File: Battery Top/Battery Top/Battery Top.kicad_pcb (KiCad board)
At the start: 2 copper layers, 64 x 21 mm, 7 parts, among them J1 JST_PWR_CON, J2 VBAT+_2, J3 VBAT+_1, J4 GND_R, J5 DATA_1, J6 GND_L

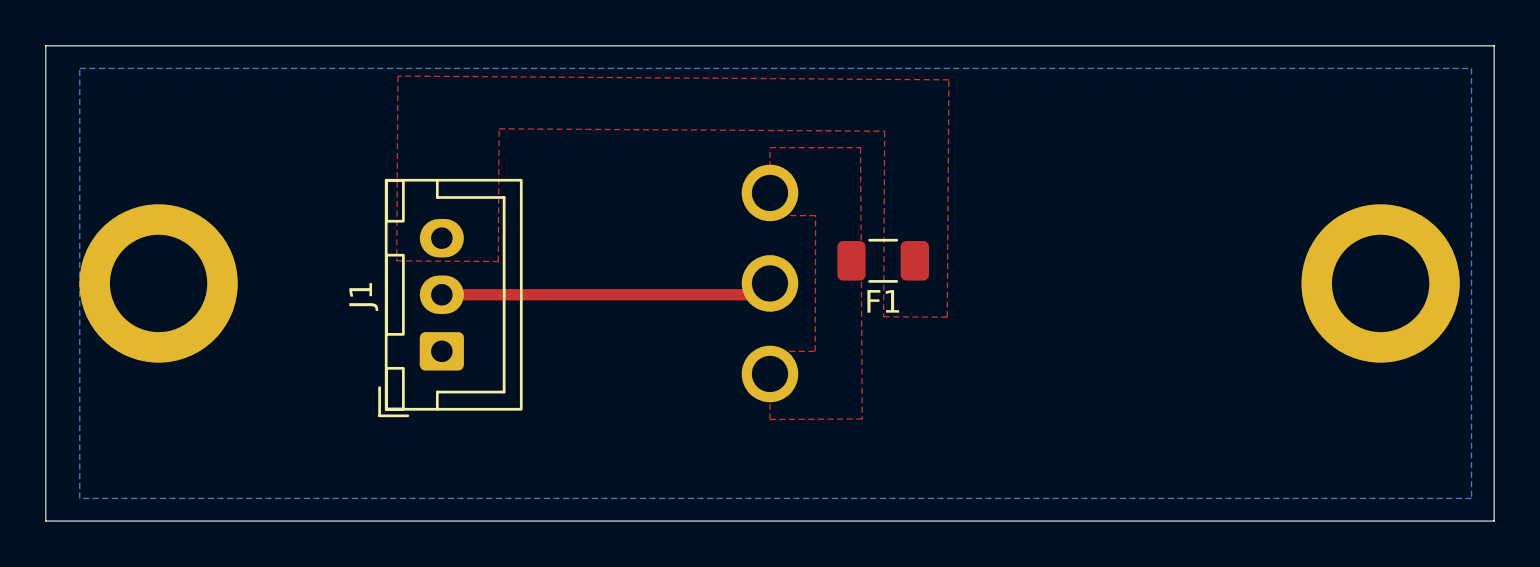
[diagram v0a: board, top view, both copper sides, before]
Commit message: fixed footprint for fuse
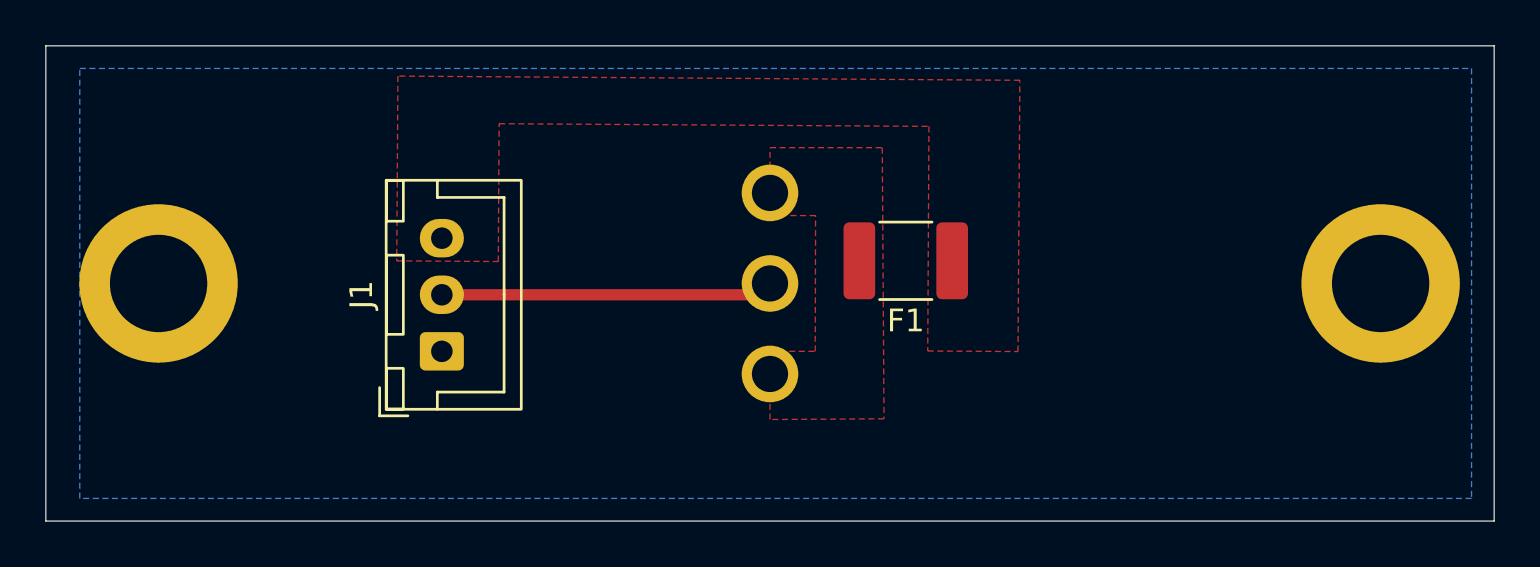
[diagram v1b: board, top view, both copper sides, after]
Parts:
- F1: footprint Fuse:Fuse_1206_3216Metric -> Capacitor_SMD:C_1812_4532Metric
- moved F1 1.00 mm to (157.0, 99.0)
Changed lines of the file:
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@@
 		)
 	)
-	(footprint "Fuse:Fuse_1206_3216Metric"
-		(layer "F.Cu")
-		(at 156 99 180)
-		(descr "Fuse SMD 1206 (3216 Metric), square (rectangular) end terminal, IPC-7351 nominal, (Body size source: http://www.tortai-tech.com/upload/download/2011102023233369053.pdf)")
-		(tags "fuse")
+	(footprint "Capacitor_SMD:C_1812_4532Metric"
+		(layer "F.Cu")
+		(at 157 99 180)
+		(descr "Capacitor SMD 1812 (4532 Metric), square (rectangular) end terminal, IPC-7351 nominal, (Body size source: IPC-SM-782 page 76, https://www.pcb-3d.com/wordpress/wp-content/uploads/ipc-sm-782a_amendment_1_and_2.pdf)")
+		(tags "capacitor")
 		(property "Reference" "F1"
-			(at 0 -1.83 180)
+			(at 0 -2.65 180)
 			(layer "F.SilkS")
 			(effects
@@
 		)
 		(property "Value" "FUSE_VBAT+_1"
-			(at 0 1.83 180)
+			(at 0 2.65 180)
 			(layer "F.Fab")
 			(effects
@@
 		(duplicate_pad_numbers_are_jumpers no)
 		(fp_line
-			(start -0.602064 0.91)
-			(end 0.602064 0.91)
+			(start -1.161252 1.71)
+			(end 1.161252 1.71)
 			(stroke
 				(width 0.12)
@@
 		)
 		(fp_line
-			(start -0.602064 -0.91)
-			(end 0.602064 -0.91)
+			(start -1.161252 -1.71)
+			(end 1.161252 -1.71)
 			(stroke
 				(width 0.12)
@@
 		)
 		(fp_rect
-			(start -2.28 -1.13)
-			(end 2.28 1.13)
+			(start -3 -1.95)
+			(end 3 1.95)
 			(stroke
 				(width 0.05)
@@
 		)
 		(fp_rect
-			(start -1.6 -0.8)
-			(end 1.6 0.8)
+			(start -2.25 -1.6)
+			(end 2.25 1.6)
 			(stroke
 				(width 0.1)
@@
 			(effects
 				(font
-					(size 0.8 0.8)
-					(thickness 0.12)
+					(size 1 1)
+					(thickness 0.15)
 				)
 			)
 		)
 		(pad "1" smd roundrect
-			(at -1.4 0 180)
-			(size 1.25 1.75)
+			(at -2.05 0 180)
+			(size 1.4 3.4)
 			(layers "F.Cu" "F.Mask" "F.Paste")
-			(roundrect_rratio 0.2)
+			(roundrect_rratio 0.178571)
 			(net "/VBAT+")
 			(pintype "passive")
 		)
 		(pad "2" smd roundrect
-			(at 1.4 0 180)
-			(size 1.25 1.75)
+			(at 2.05 0 180)
+			(size 1.4 3.4)
 			(layers "F.Cu" "F.Mask" "F.Paste")
-			(roundrect_rratio 0.2)
+			(roundrect_rratio 0.178571)
 			(net "/VBAT+_P")
 			(pintype "passive")
 		)
 		(embedded_fonts no)
-		(model "${KICAD10_3DMODEL_DIR}/Fuse.3dshapes/Fuse_1206_3216Metric.step"
+		(model "${KICAD10_3DMODEL_DIR}/Capacitor_SMD.3dshapes/C_1812_4532Metric.step"
 			(offset
 				(xyz 0 0 0)
@@
 		(polygon
 			(pts
-				(xy 153.01436 97.00265) (xy 151 96.997387) (xy 151 94) (xy 155 94) (xy 155.076836 105.986685) (xy 151 106.012822)
-				(xy 151 103.000002) (xy 152.998694 103)
+				(xy 153.01436 97.00265) (xy 151 96.997387) (xy 151 94) (xy 155.96154 94) (xy 156.038336 105.980521)
+				(xy 151 106.012822) (xy 151 103.000002) (xy 152.998694 103)
 			)
 		)
@@
 		(polygon
 			(pts
-				(xy 156.065616 93.272563) (xy 156.021234 101.473358) (xy 158.832609 101.490425) (xy 158.904102 91.001759)
-				(xy 134.558549 90.837635) (xy 134.506528 99.002706) (xy 138.993546 99.031294) (xy 139.029647 93.167675)
-			)
-		)
+				(xy 158.024037 93.058638) (xy 157.970318 102.985172) (xy 161.959035 103.009294) (xy 162.040744 91.023)
+				(xy 134.558549 90.837635) (xy 134.506528 99.002706) (xy 138.993546 99.031294) (xy 139.031038 92.941701)
+			)
+		)
